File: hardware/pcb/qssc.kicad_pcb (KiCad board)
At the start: 6 copper layers, 210 x 140 mm, 386 parts, among them J1 FT232RL, J10 USB-C, J2 5V Barrel, J3 SMA, J4 12V LED, J7 RESET, J8 MW_GATE, J9 JTAG, U1 XC7A35T-1CSG324C, U3 ADF4351BCPZ, U5 GVA-84+, U8 W25Q128JVSIQ, Y1 100MHz TCXO

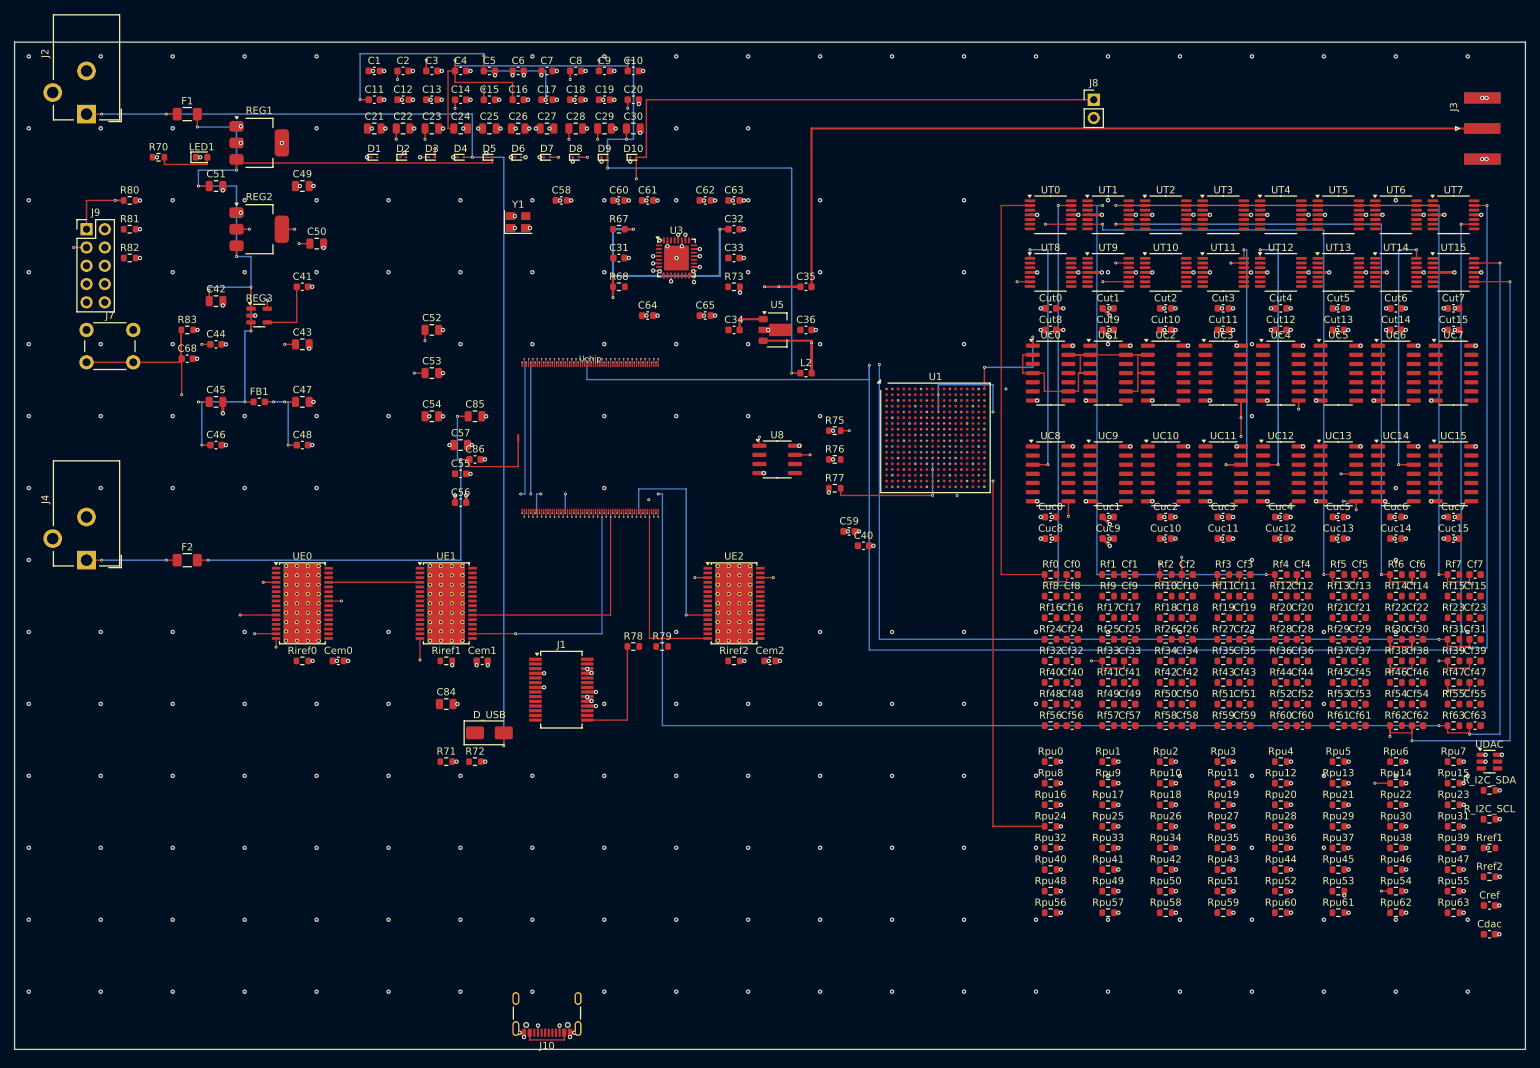
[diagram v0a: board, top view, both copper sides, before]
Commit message: pcb: DRC 0/0/0 — exclude chip nets from line router, fix straggler-via shorts
Two final DRC violation classes closed; the merged board is now violation-clean
(unconnected_items ignored per the first-pass-router convention).

- route_signals: skip all 128 chip nets (DET_IN*, emitter_cat*) in the signal
  loop -> fail/unrouted. The 0.30 mm-pitch dog-bone field is beyond the 0.2 mm
  line-router grid: each dog-bone via marks a radius-2 (5-cell) block, and
  same-parity vias sit only 0.60 mm (3 cells) apart, so their mark blocks
  overlap by 2 cells; the own-keepout `allowed` override then lets a net claim
  that overlap and route into the neighbour's via copper (DET_IN62 escape
  0.025 mm from DET_IN60's via on In3.Cu). _chip_fanout's dog-bone (pad ->
  0.15 mm stub -> through-via) is itself DRC-clean and is preserved by the
  chip_via_pos guard; only the via<->target escape is left to FreeRouting
  (Task 17), which routes continuous copper and respects the 0.10 mm Chip
  clearance. Routed 39 -> 29/317 (the ~10 partially-routed chip nets rejoin
  the honest UNROUTED set, now 284).
- route_qssc_pcb: the +5V straggler B.Cu L-trace crossed just-placed GND/+3V3
  rail-pad vias (a decoupling-cap bank row at y=4) -> 5 shorting_items. The
  straggler tie's obstacle set (obs_circles) is snapshotted BEFORE _clear_routed,
  so it cannot see vias placed later in the same build() run. Thread the
  via_centers list (surviving + rail-pad + stitching vias, with netcodes)
  into _bcu_seg_clear so the L-trace also clears run-placed vias. DRC 5 -> 0.

DRC on the routed merged board: 0 violations, 0 unconnected (test_pcb_drc
passes). Down from 43 (TLC5947 redesign) -> 13 -> 2 -> 0.

Co-Authored-By: Claude Code <noreply@anthropic.com>
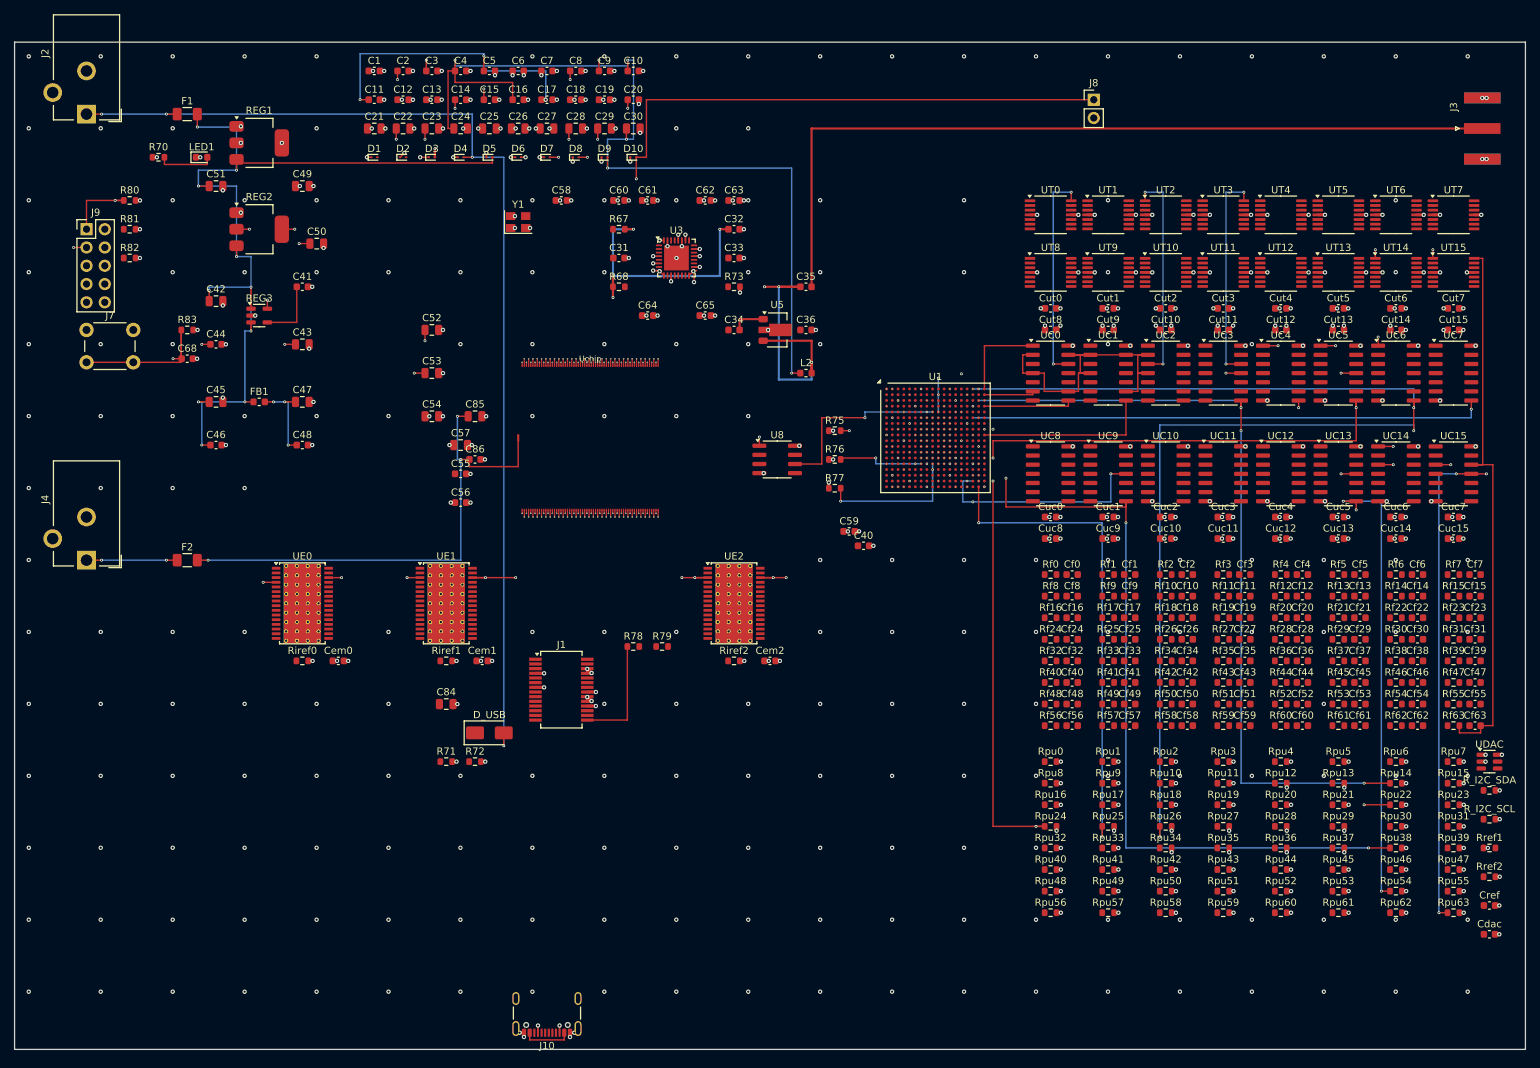
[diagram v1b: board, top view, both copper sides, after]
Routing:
- net DET_IN7: track 268.4 -> 1.00 mm, vias 4 -> 1
- net DET_IN6: track 247.9 -> 0.50 mm, vias 4 -> 1
- net DET_IN62: track 247.6 -> 0.50 mm, vias 5 -> 1
- net DET_IN63: track 241.7 -> 1.00 mm, vias 5 -> 1
- net DET_IN30: track 232.0 -> 0.50 mm, vias 5 -> 1
- net DET_IN31: track 232.5 -> 1.00 mm, vias 5 -> 1
- net DET_IN4: track 222.9 -> 0.50 mm, vias 5 -> 1
- net DET_IN2: track 196.7 -> 0.50 mm, vias 5 -> 1
- net DET_DIG26: track 0.00 -> 164.0 mm, vias 0 -> 4
- net DET_DIG63: track 0.00 -> 148.8 mm, vias 0 -> 4
- net DET_DIG22: track 0.00 -> 124.0 mm, vias 0 -> 4
- net DET_DIG24: track 57.2 -> 175.1 mm, vias 1 -> 4
- net DET_DIG38: track 0.00 -> 111.4 mm, vias 0 -> 4
- net DET_IN39: track 109.3 -> 1.00 mm, vias 3 -> 1
- net DET_IN38: track 104.8 -> 0.50 mm, vias 3 -> 1
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
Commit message: pcb: two-board sandwich routed + DRC/ERC 0/0, HDI via rules
Split the single merged board into the production two-PCB sandwich for the
two-faced (no-TSV) QSSC die:

- Main board (qssc, 6-layer 210x140): FPGA + 3x TLC5947 emitter + RF + USB +
  power, die BOTTOM/emitter face on F.Cu (ACF pressure contact), BTB HOST J12.
- Detector head (chip_module, 4-layer 150x140): 16x TLV9004 TIA + 4x AD7616
  ADC, die TOP/detector face on B.Cu+B.Mask (no B.Paste), BTB DAUGHTER J12.
  Head origin = main origin + (60,0)mm so J12 and die footprints align.
- BTB J12 carries the 9-wire AD7616 SPI + GND/+3V3/+5V; identical net names
  on both boards. RTL and Qiskit software unchanged.

Generator (gen_qssc_kicad.py): parameterized emit_schematic/emit_pcb/emit_pro
on a per-board cfg; HEAD_LAYER_STACK/HEAD_STACK_UP/HEAD_CFG + build_detector_head
+ assign_pcb_positions_head; split chip face into QSSC_Chip_EM (F.Cu) /
QSSC_Chip_DET (B.Cu); authored Conn_02x10_BTB; main() emits both boards.
emit_pro design rules now match the HDI stackup: min_via_diameter 0.45->0.20,
min_via_annular_width 0.10->0.05 (agrees with route_signals
_relax_board_for_hdi: 0.20 mm VIP / 0.05 mm via-in-pad annular). The old
0.45/0.10 floor flagged every routing (0.40 mm) and BGA dog-bone (0.20 mm)
via as via_diameter/annular_width.

Router (route_signals.py): SIGNAL/PLANE/JUMP layers recomputed from
GetCopperLayerCount (4-layer head safe); _chip_fanout stub/escape derived
from the pad's own layer (DET pads escape on F.Cu, EM pads on B.Cu); _FpProxy
stores x,y so the snapshot proxy has a position.

Result (fresh gen -> route_signals -> route_qssc_pcb -> kicad-cli):
  qssc        DRC 0 violations, ERC 0 errors
  chip_module DRC 0 violations, ERC 0 errors
Main: 26/130 nets 1st-pass + 2 planes (GND/+3V3) + 398 vias; 100 unrouted
(64 emitter cathodes + FPGA config/RF/USB) left for FreeRouting.
Head: 10/156 nets 1st-pass + 2 planes + 435 vias; 146 unrouted (DET->TIA->
ADC analog + SPI) left for FreeRouting.

Co-Authored-By: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
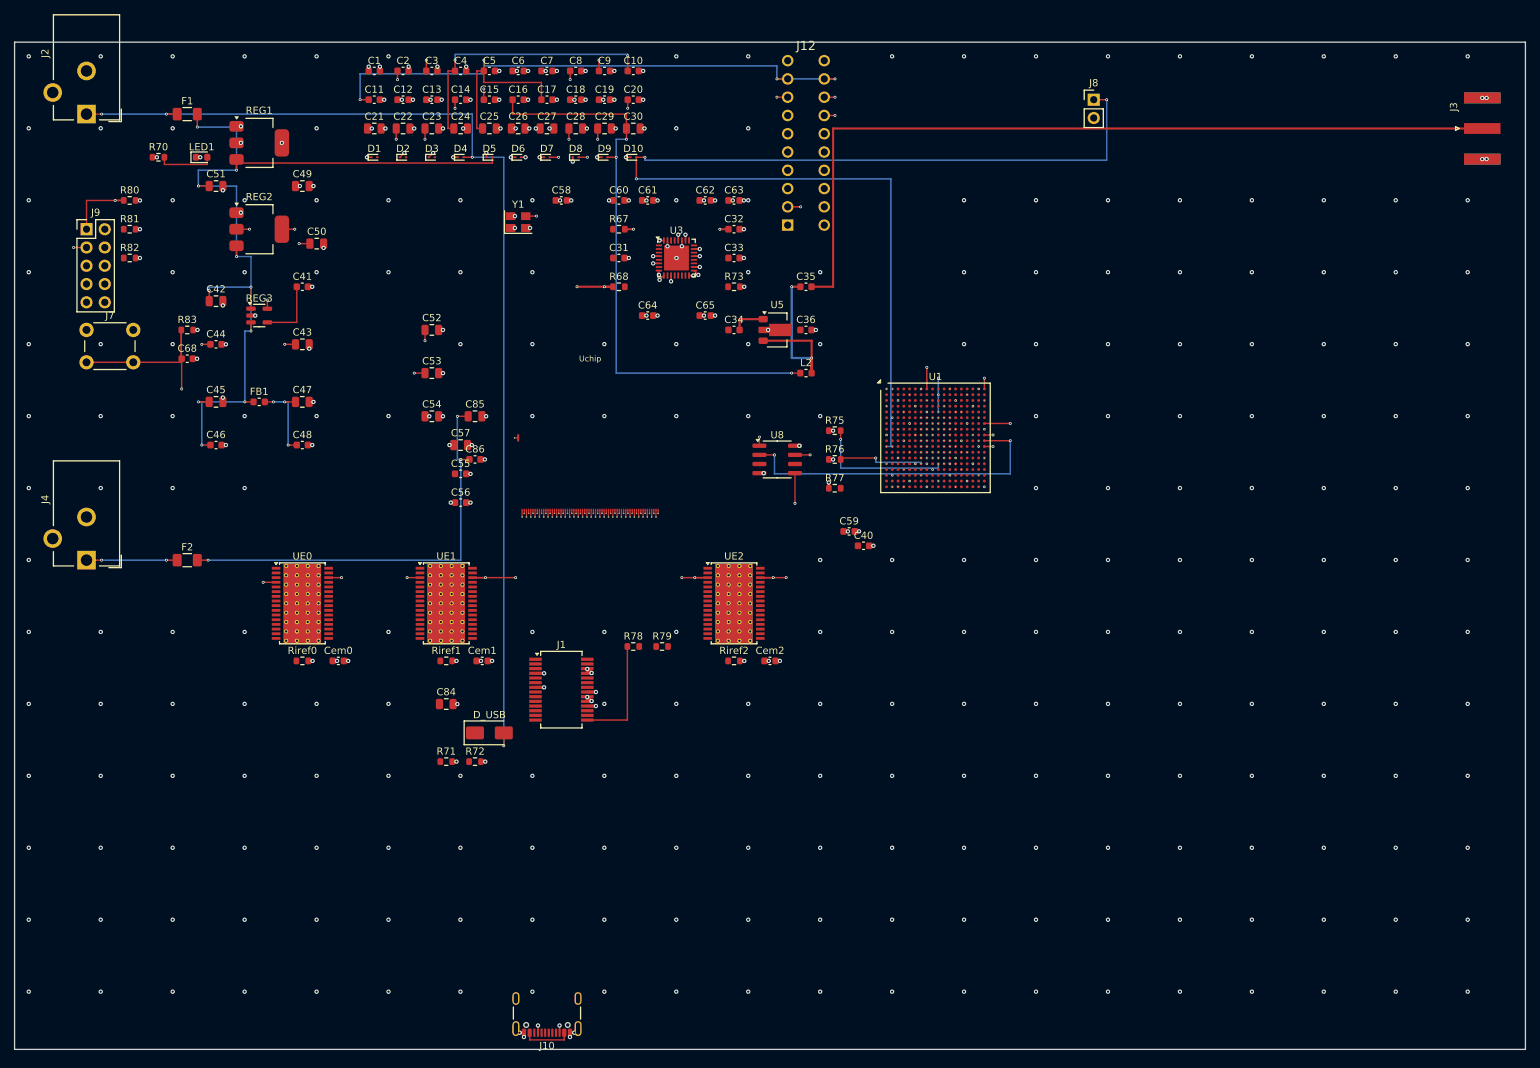
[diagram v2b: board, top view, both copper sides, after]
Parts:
- removed Cdac, Cref, Cuc0, Cuc1, Cuc10, Cuc11, Cuc12, Cuc13, Cuc14, Cuc15, Cuc2, Cuc3, Cuc4, Cuc5, Cuc6, Cuc7, Cuc8, Cuc9, Cut0, Cut1, Cut10, Cut11, Cut12, Cut13, Cut14, Cut15, Cut2, Cut3, Cut4, Cut5, Cut6, Cut7, Cut8, Cut9: 100nF, C_0603_1608Metric
- removed Cf0, Cf1, Cf10, Cf11, Cf12, Cf13, Cf14, Cf15, Cf16, Cf17, Cf18, Cf19, Cf2, Cf20, Cf21, Cf22, Cf23, Cf24, Cf25, Cf26, Cf27, Cf28, Cf29, Cf3, Cf30, Cf31, Cf32, Cf33, Cf34, Cf35, Cf36, Cf37, Cf38, Cf39, Cf4, Cf40, Cf41, Cf42, Cf43, Cf44, Cf45, Cf46, Cf47, Cf48, Cf49, Cf5, Cf50, Cf51, Cf52, Cf53, Cf54, Cf55, Cf56, Cf57, Cf58, Cf59, Cf6, Cf60, Cf61, Cf62, Cf63, Cf7, Cf8, Cf9: 1pF, C_0603_1608Metric
- removed R_I2C_SCL, R_I2C_SDA: 4.7k, R_0603_1608Metric
- removed Rf0, Rf1, Rf10, Rf11, Rf12, Rf13, Rf14, Rf15, Rf16, Rf17, Rf18, Rf19, Rf2, Rf20, Rf21, Rf22, Rf23, Rf24, Rf25, Rf26, Rf27, Rf28, Rf29, Rf3, Rf30, Rf31, Rf32, Rf33, Rf34, Rf35, Rf36, Rf37, Rf38, Rf39, Rf4, Rf40, Rf41, Rf42, Rf43, Rf44, Rf45, Rf46, Rf47, Rf48, Rf49, Rf5, Rf50, Rf51, Rf52, Rf53, Rf54, Rf55, Rf56, Rf57, Rf58, Rf59, Rf6, Rf60, Rf61, Rf62, Rf63, Rf7, Rf8, Rf9: 1M, R_0603_1608Metric
- removed Rpu0, Rpu1, Rpu10, Rpu11, Rpu12, Rpu13, Rpu14, Rpu15, Rpu16, Rpu17, Rpu18, Rpu19, Rpu2, Rpu20, Rpu21, Rpu22, Rpu23, Rpu24, Rpu25, Rpu26, Rpu27, Rpu28, Rpu29, Rpu3, Rpu30, Rpu31, Rpu32, Rpu33, Rpu34, Rpu35, Rpu36, Rpu37, Rpu38, Rpu39, Rpu4, Rpu40, Rpu41, Rpu42, Rpu43, Rpu44, Rpu45, Rpu46, Rpu47, Rpu48, Rpu49, Rpu5, Rpu50, Rpu51, Rpu52, Rpu53, Rpu54, Rpu55, Rpu56, Rpu57, Rpu58, Rpu59, Rpu6, Rpu60, Rpu61, Rpu62, Rpu63, Rpu7, Rpu8, Rpu9, Rref1, Rref2: 10k, R_0603_1608Metric
- removed UC0, UC1, UC10, UC11, UC12, UC13, UC14, UC15, UC2, UC3, UC4, UC5, UC6, UC7, UC8, UC9: LMV339, SOIC-14_3.9x8.7mm_P1.27mm
- removed UDAC: MCP4725, SOT-23-6
- removed UT0, UT1, UT10, UT11, UT12, UT13, UT14, UT15, UT2, UT3, UT4, UT5, UT6, UT7, UT8, UT9: TLV9004, TSSOP-14_4.4x5mm_P0.65mm
- removed the Uchip at (80.0, 55.0)
- added J12: BTB_HOST, qssc:Conn_02x10_BTB, F.Cu at (110.0, 14.0)
- added Uchip: QSSC_Chip_EM, qssc:QSSC_Chip_EM, F.Cu at (80.0, 55.0)
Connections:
- U1 pad A14: DET_DIG55 -> (no net)
- U1 pad A15: DET_DIG41 -> (no net)
- U1 pad A16: DET_DIG26 -> (no net)
- U1 pad A18: DET_DIG0 -> adc_convst
- U1 pad B14: DET_DIG56 -> (no net)
- U1 pad B16: DET_DIG27 -> (no net)
- U1 pad B17: DET_DIG13 -> (no net)
- U1 pad B18: DET_DIG1 -> adc_sclk
- U1 pad C14: DET_DIG57 -> (no net)
- U1 pad C15: DET_DIG42 -> (no net)
- U1 pad C16: DET_DIG28 -> (no net)
- U1 pad C17: DET_DIG14 -> (no net)
- U1 pad D14: DET_DIG58 -> (no net)
- U1 pad D15: DET_DIG43 -> (no net)
- U1 pad D17: DET_DIG15 -> (no net)
- U1 pad D18: DET_DIG2 -> adc_miso
- U1 pad E15: DET_DIG44 -> (no net)
- U1 pad E16: DET_DIG29 -> (no net)
- U1 pad E17: DET_DIG16 -> (no net)
- U1 pad E18: DET_DIG3 -> adc_busy
- U1 pad F14: DET_DIG59 -> (no net)
- U1 pad F15: DET_DIG45 -> (no net)
- U1 pad F16: DET_DIG30 -> (no net)
- U1 pad F18: DET_DIG4 -> adc_cs0
- U1 pad G14: DET_DIG60 -> (no net)
- U1 pad G16: DET_DIG31 -> (no net)
- U1 pad G17: DET_DIG17 -> (no net)
- U1 pad G18: DET_DIG5 -> adc_cs1
- U1 pad H14: DET_DIG61 -> (no net)
- U1 pad H15: DET_DIG46 -> (no net)
- U1 pad H16: DET_DIG32 -> (no net)
- U1 pad H17: DET_DIG18 -> (no net)
- U1 pad J14: DET_DIG62 -> (no net)
- U1 pad J15: DET_DIG47 -> (no net)
- U1 pad J17: DET_DIG19 -> (no net)
- U1 pad J18: DET_DIG6 -> adc_cs2
- U1 pad K15: DET_DIG48 -> (no net)
- U1 pad K16: DET_DIG33 -> (no net)
- U1 pad L15: DET_DIG49 -> (no net)
- U1 pad L16: DET_DIG34 -> (no net)
- U1 pad L18: DET_DIG7 -> adc_cs3
- U1 pad M1: I2C_SDA -> (no net)
- U1 pad M16: DET_DIG35 -> (no net)
- U1 pad M17: DET_DIG20 -> (no net)
- U1 pad M18: DET_DIG8 -> adc_resetn
- U1 pad N1: I2C_SCL -> (no net)
- U1 pad N14: DET_DIG63 -> (no net)
- U1 pad N15: DET_DIG50 -> (no net)
- U1 pad N16: DET_DIG36 -> (no net)
- U1 pad N17: DET_DIG21 -> (no net)
- U1 pad P15: DET_DIG51 -> (no net)
- U1 pad P17: DET_DIG22 -> (no net)
- U1 pad P18: DET_DIG9 -> (no net)
- U1 pad R15: DET_DIG52 -> (no net)
- U1 pad R16: DET_DIG37 -> (no net)
- U1 pad R17: DET_DIG23 -> (no net)
- U1 pad R18: DET_DIG10 -> (no net)
- U1 pad T15: DET_DIG53 -> (no net)
- U1 pad T16: DET_DIG38 -> (no net)
- U1 pad T18: DET_DIG11 -> (no net)
- U1 pad U16: DET_DIG39 -> (no net)
- U1 pad U17: DET_DIG24 -> (no net)
- U1 pad U18: DET_DIG12 -> (no net)
- U1 pad V15: DET_DIG54 -> (no net)
- U1 pad V16: DET_DIG40 -> (no net)
- U1 pad V17: DET_DIG25 -> (no net)
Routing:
- net DET_DIG24: track 175.1 -> 0.00 mm, vias 4 -> 0
- net DET_DIG26: track 164.0 -> 0.00 mm, vias 4 -> 0
- net DET_DIG63: track 148.8 -> 0.00 mm, vias 4 -> 0
- net DET_DIG22: track 124.0 -> 0.00 mm, vias 4 -> 0
- net DET_DIG54: track 121.0 -> 0.00 mm, vias 4 -> 0
- net DET_DIG14: track 112.4 -> 0.00 mm, vias 4 -> 0
- net DET_DIG38: track 111.4 -> 0.00 mm, vias 4 -> 0
- net DET_DIG56: track 88.3 -> 0.00 mm, vias 2 -> 0
- net +3V3: track 116.5 -> 29.7 mm, vias 208 -> 76
- net clk_100mhz: track 0.00 -> 79.8 mm, vias 0 -> 2
- net adc_cs2: track 0.00 -> 79.7 mm, vias 0 -> 2
- net RF_AMP_OUT: track 106.8 -> 27.2 mm, vias 4 -> 2
- net DET_TIA63: track 77.4 -> 0.00 mm
- net adc_cs3: track 0.00 -> 74.8 mm, vias 0 -> 2
- net adc_cs1: track 0.00 -> 72.3 mm, vias 0 -> 2
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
